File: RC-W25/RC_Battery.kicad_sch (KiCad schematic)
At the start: 18 parts, among them P1 JST CONN, SW1 Toggle Button, U2 MCP73831-5-OT, U3 AP62300TWU

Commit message: Began Routing
Only need to spec out buttons before completion
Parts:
- L1: footprint Inductor_SMD:ASPI-4030S-330M-T -> Inductor_SMD:L_Abracon_ASPI-4030S; LCSC# (none) -> C2050508
- renumbered R9 to R10, R10 to R11, R11 to R12, R12 to R13, R13 to R14, R8 to R9, SW1 to SW3
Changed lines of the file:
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@@
 		(on_board yes)
 		(dnp no)
-		(property "Reference" "#PWR028"
+		(property "Reference" "#PWR030"
 			(at 52.07 73.66 0)
 			(effects
@@
 			(project ""
 				(path "/427b2895-e3a6-4096-b101-5f65a3f7473e/9423f10d-7c89-4a48-b233-1b4f9ab13c89"
-					(reference "#PWR028")
+					(reference "#PWR030")
 					(unit 1)
 				)
@@
 		(on_board yes)
 		(dnp no)
-		(property "Reference" "R8"
+		(property "Reference" "R9"
 			(at 59.182 79.248 0)
 			(effects
@@
 			(project "RC-W25"
 				(path "/427b2895-e3a6-4096-b101-5f65a3f7473e/9423f10d-7c89-4a48-b233-1b4f9ab13c89"
-					(reference "R8")
+					(reference "R9")
 					(unit 1)
 				)
@@
 		(dnp no)
 		(fields_autoplaced yes)
-		(property "Reference" "#PWR027"
+		(property "Reference" "#PWR029"
 			(at 52.07 63.5 0)
 			(effects
@@
 			(project ""
 				(path "/427b2895-e3a6-4096-b101-5f65a3f7473e/9423f10d-7c89-4a48-b233-1b4f9ab13c89"
-					(reference "#PWR027")
+					(reference "#PWR029")
 					(unit 1)
 				)
@@
 		(dnp no)
 		(fields_autoplaced yes)
-		(property "Reference" "#PWR036"
+		(property "Reference" "#PWR038"
 			(at 176.53 133.35 0)
 			(effects
@@
 			(project "RC-W25"
 				(path "/427b2895-e3a6-4096-b101-5f65a3f7473e/9423f10d-7c89-4a48-b233-1b4f9ab13c89"
-					(reference "#PWR036")
+					(reference "#PWR038")
 					(unit 1)
 				)
@@
 		(dnp no)
 		(fields_autoplaced yes)
-		(property "Reference" "#PWR038"
+		(property "Reference" "#PWR040"
 			(at 223.52 137.16 0)
 			(effects
@@
 			(project "RC-W25"
 				(path "/427b2895-e3a6-4096-b101-5f65a3f7473e/9423f10d-7c89-4a48-b233-1b4f9ab13c89"
-					(reference "#PWR038")
+					(reference "#PWR040")
 					(unit 1)
 				)
@@
 		(on_board yes)
 		(dnp no)
-		(property "Reference" "#PWR035"
+		(property "Reference" "#PWR037"
 			(at 153.67 129.54 0)
 			(effects
@@
 			(project "RC-W25"
 				(path "/427b2895-e3a6-4096-b101-5f65a3f7473e/9423f10d-7c89-4a48-b233-1b4f9ab13c89"
-					(reference "#PWR035")
+					(reference "#PWR037")
 					(unit 1)
 				)
@@
 			)
 		)
-		(property "Footprint" "Inductor_SMD:ASPI-4030S-330M-T"
+		(property "Footprint" "Inductor_SMD:L_Abracon_ASPI-4030S"
 			(at 205.74 116.84 0)
 			(effects
@@
 			)
 		)
-		(property "Datasheet" "https://abracon.com/Magnetics/power/ASPI-4030S.pdf"
+		(property "Datasheet" "https://www.lcsc.com/datasheet/lcsc_datasheet_2410121520_Abracon-LLC-ASPI-4030S-3R3M-T_C2050508.pdf"
 			(at 205.74 116.84 0)
 			(effects
@@
 			)
 		)
-		(property "LCSC#" ""
+		(property "LCSC#" "C2050508"
 			(at 205.74 116.84 0)
 			(effects
@@
 		(dnp no)
 		(fields_autoplaced yes)
-		(property "Reference" "#PWR039"
+		(property "Reference" "#PWR041"
 			(at 234.95 116.84 0)
 			(effects
@@
 			(project "RC-W25"
 				(path "/427b2895-e3a6-4096-b101-5f65a3f7473e/9423f10d-7c89-4a48-b233-1b4f9ab13c89"
-					(reference "#PWR039")
+					(reference "#PWR041")
 					(unit 1)
 				)
@@
 		(on_board yes)
 		(dnp no)
-		(property "Reference" "R13"
+		(property "Reference" "R14"
 			(at 216.408 127.762 0)
 			(effects
@@
 			(project "RC-W25"
 				(path "/427b2895-e3a6-4096-b101-5f65a3f7473e/9423f10d-7c89-4a48-b233-1b4f9ab13c89"
-					(reference "R13")
+					(reference "R14")
 					(unit 1)
 				)
@@
 		(on_board yes)
 		(dnp no)
-		(property "Reference" "#PWR032"
+		(property "Reference" "#PWR034"
 			(at 128.27 97.79 0)
 			(effects
@@
 			(project "RC-W25"
 				(path "/427b2895-e3a6-4096-b101-5f65a3f7473e/9423f10d-7c89-4a48-b233-1b4f9ab13c89"
-					(reference "#PWR032")
+					(reference "#PWR034")
 					(unit 1)
 				)
@@
 		(on_board yes)
 		(dnp no)
-		(property "Reference" "R9"
+		(property "Reference" "R10"
 			(at 68.326 78.994 0)
 			(effects
@@
 			(project "RC-W25"
 				(path "/427b2895-e3a6-4096-b101-5f65a3f7473e/9423f10d-7c89-4a48-b233-1b4f9ab13c89"
-					(reference "R9")
+					(reference "R10")
 					(unit 1)
 				)
@@
 		(on_board yes)
 		(dnp no)
-		(property "Reference" "R10"
+		(property "Reference" "R11"
 			(at 123.698 75.692 0)
 			(effects
@@
 			(project "RC-W25"
 				(path "/427b2895-e3a6-4096-b101-5f65a3f7473e/9423f10d-7c89-4a48-b233-1b4f9ab13c89"
-					(reference "R10")
+					(reference "R11")
 					(unit 1)
 				)
@@
 		(dnp no)
 		(fields_autoplaced yes)
-		(property "Reference" "#PWR034"
+		(property "Reference" "#PWR036"
 			(at 147.32 118.11 0)
 			(effects
@@
 			(project "RC-W25"
 				(path "/427b2895-e3a6-4096-b101-5f65a3f7473e/9423f10d-7c89-4a48-b233-1b4f9ab13c89"
-					(reference "#PWR034")
+					(reference "#PWR036")
 					(unit 1)
 				)
@@
 		(on_board yes)
 		(dnp no)
-		(property "Reference" "SW1"
+		(property "Reference" "SW3"
 			(at 116.84 59.944 90)
 			(effects
@@
 			(project ""
 				(path "/427b2895-e3a6-4096-b101-5f65a3f7473e/9423f10d-7c89-4a48-b233-1b4f9ab13c89"
-					(reference "SW1")
+					(reference "SW3")
 					(unit 1)
 				)
@@
 		(on_board yes)
 		(dnp no)
-		(property "Reference" "R12"
+		(property "Reference" "R13"
 			(at 216.408 120.142 0)
 			(effects
@@
 			(project "RC-W25"
 				(path "/427b2895-e3a6-4096-b101-5f65a3f7473e/9423f10d-7c89-4a48-b233-1b4f9ab13c89"
-					(reference "R12")
+					(reference "R13")
 					(unit 1)
 				)
@@
 		(on_board yes)
 		(dnp no)
-		(property "Reference" "#PWR030"
+		(property "Reference" "#PWR032"
 			(at 105.41 83.82 0)
 			(effects
@@
 			(project "RC-W25"
 				(path "/427b2895-e3a6-4096-b101-5f65a3f7473e/9423f10d-7c89-4a48-b233-1b4f9ab13c89"
-					(reference "#PWR030")
+					(reference "#PWR032")
 					(unit 1)
 				)
@@
 		(on_board yes)
 		(dnp no)
-		(property "Reference" "#PWR029"
+		(property "Reference" "#PWR031"
 			(at 72.39 91.44 0)
 			(effects
@@
 			(project ""
 				(path "/427b2895-e3a6-4096-b101-5f65a3f7473e/9423f10d-7c89-4a48-b233-1b4f9ab13c89"
-					(reference "#PWR029")
+					(reference "#PWR031")
 					(unit 1)
 				)
@@
 		(on_board yes)
 		(dnp no)
-		(property "Reference" "#PWR031"
+		(property "Reference" "#PWR033"
 			(at 115.57 59.69 0)
 			(effects
@@
 			(project "RC-W25"
 				(path "/427b2895-e3a6-4096-b101-5f65a3f7473e/9423f10d-7c89-4a48-b233-1b4f9ab13c89"
-					(reference "#PWR031")
+					(reference "#PWR033")
 					(unit 1)
 				)
@@
 		(dnp no)
 		(fields_autoplaced yes)
-		(property "Reference" "#PWR037"
+		(property "Reference" "#PWR039"
 			(at 214.63 137.16 0)
 			(effects
@@
 			(project "RC-W25"
 				(path "/427b2895-e3a6-4096-b101-5f65a3f7473e/9423f10d-7c89-4a48-b233-1b4f9ab13c89"
-					(reference "#PWR037")
+					(reference "#PWR039")
 					(unit 1)
 				)
@@
 		(dnp no)
 		(fields_autoplaced yes)
-		(property "Reference" "#PWR040"
+		(property "Reference" "#PWR042"
 			(at 234.95 137.16 0)
 			(effects
@@
 			(project "RC-W25"
 				(path "/427b2895-e3a6-4096-b101-5f65a3f7473e/9423f10d-7c89-4a48-b233-1b4f9ab13c89"
-					(reference "#PWR040")
+					(reference "#PWR042")
 					(unit 1)
 				)
@@
 		(on_board yes)
 		(dnp no)
-		(property "Reference" "R11"
+		(property "Reference" "R12"
 			(at 123.698 85.598 0)
 			(effects
@@
 			(project "RC-W25"
 				(path "/427b2895-e3a6-4096-b101-5f65a3f7473e/9423f10d-7c89-4a48-b233-1b4f9ab13c89"
-					(reference "R11")
+					(reference "R12")
 					(unit 1)
 				)
@@
 		(on_board yes)
 		(dnp no)
-		(property "Reference" "#PWR053"
+		(property "Reference" "#PWR035"
 			(at 140.97 78.74 0)
 			(effects
@@
 			(project "RC-W25"
 				(path "/427b2895-e3a6-4096-b101-5f65a3f7473e/9423f10d-7c89-4a48-b233-1b4f9ab13c89"
-					(reference "#PWR053")
-					(unit 1)
-				)
+					(reference "#PWR035")
+					(unit 1)
+				)

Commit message: EM Custom RC V1
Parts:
- removed SW3: Toggle Button, symbol Switch:SW_SPST
- added SW5: YTSPS-22E58LM, footprints:SW-SMD_6P-YTSPS-22E58LM, symbol components:YTSPS-22E58LM
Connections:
- net +VBAT: now also SW5.2
- net at C11.1, P1.1 (Pin_1), R11.1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: now also SW5.3
- no-connect marks 1 -> 5

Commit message: crc v1
finalized!! finally!! yes!!

- spec out 3.7V 1000mAh cell
- spec out ultra-thin coin motor

^make sure they have a jst-ph male connector or are organized to be ordered alongside one for manual soldering.
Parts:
- P1: footprint Library:CONN02_502352_MOL -> footprints:CONN-SMD_2P-P2.00_XUNPU_WAFER-PH2.0-2PWB; LCSC# (none) -> C3029440
- renumbered SW5 to SW3
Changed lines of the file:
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@@
 			)
 		)
-		(property "Footprint" "Library:CONN02_502352_MOL"
+		(property "Footprint" "footprints:CONN-SMD_2P-P2.00_XUNPU_WAFER-PH2.0-2PWB"
 			(at 146.05 69.85 0)
 			(effects
@@
 			)
 		)
-		(property "Datasheet" "~"
+		(property "Datasheet" "https://www.lcsc.com/datasheet/lcsc_datasheet_2411192313_XUNPU-WAFER-PH2-0-2PWB_C3029440.pdf"
 			(at 146.05 69.85 0)
 			(effects
@@
 			)
 		)
-		(property "LCSC#" ""
+		(property "LCSC#" "C3029440"
 			(at 146.05 69.85 0)
 			(effects
@@
 		(on_board yes)
 		(dnp no)
-		(property "Reference" "SW5"
+		(property "Reference" "SW3"
 			(at 126.746 60.452 90)
 			(effects
@@
 			(project ""
 				(path "/427b2895-e3a6-4096-b101-5f65a3f7473e/9423f10d-7c89-4a48-b233-1b4f9ab13c89"
-					(reference "SW5")
-					(unit 1)
-				)
+					(reference "SW3")
+					(unit 1)
+				)

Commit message: crc v1
quick fixes
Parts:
- L1: footprint Inductor_SMD:L_Abracon_ASPI-4030S -> footprints:L_Abracon_ASPI-4030S
- R11: value 42k -> 36.6k
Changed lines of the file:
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@@
 	)
 	(symbol
-		(lib_id "power:GND")
+		(lib_id "power:Earth")
 		(at 52.07 67.31 0)
 		(unit 1)
@@
 			)
 		)
-		(property "Datasheet" ""
+		(property "Datasheet" "~"
 			(at 52.07 67.31 0)
 			(effects
@@
 			)
 		)
-		(property "Description" "Power symbol creates a global label with name \"GND\" , ground"
+		(property "Description" "Power symbol creates a global label with name \"Earth\""
 			(at 52.07 67.31 0)
 			(effects
@@
 	)
 	(symbol
-		(lib_id "power:GND")
+		(lib_id "power:Earth")
 		(at 176.53 127 0)
 		(unit 1)
@@
 		)
 		(property "Value" "GND"
-			(at 176.53 132.08 0)
-			(effects
-				(font
-					(size 1.27 1.27)
-				)
+			(at 179.07 128.2699 0)
+			(effects
+				(font
+					(size 1.27 1.27)
+				)
+				(justify left)
 			)
 		)
@@
 			)
 		)
-		(property "Datasheet" ""
+		(property "Datasheet" "~"
 			(at 176.53 127 0)
 			(effects
@@
 			)
 		)
-		(property "Description" "Power symbol creates a global label with name \"GND\" , ground"
+		(property "Description" "Power symbol creates a global label with name \"Earth\""
 			(at 176.53 127 0)
 			(effects
@@
 	)
 	(symbol
-		(lib_id "power:GND")
+		(lib_id "power:Earth")
 		(at 223.52 130.81 0)
 		(unit 1)
@@
 		)
 		(property "Value" "GND"
-			(at 223.52 135.89 0)
-			(effects
-				(font
-					(size 1.27 1.27)
-				)
+			(at 226.06 132.0799 0)
+			(effects
+				(font
+					(size 1.27 1.27)
+				)
+				(justify left)
 			)
 		)
@@
 			)
 		)
-		(property "Datasheet" ""
+		(property "Datasheet" "~"
 			(at 223.52 130.81 0)
 			(effects
@@
 			)
 		)
-		(property "Description" "Power symbol creates a global label with name \"GND\" , ground"
+		(property "Description" "Power symbol creates a global label with name \"Earth\""
 			(at 223.52 130.81 0)
 			(effects
@@
 	)
 	(symbol
-		(lib_id "power:GND")
+		(lib_id "power:Earth")
 		(at 153.67 123.19 0)
 		(unit 1)
@@
 			)
 		)
-		(property "Datasheet" ""
+		(property "Datasheet" "~"
 			(at 153.67 123.19 0)
 			(effects
@@
 			)
 		)
-		(property "Description" "Power symbol creates a global label with name \"GND\" , ground"
+		(property "Description" "Power symbol creates a global label with name \"Earth\""
 			(at 153.67 123.19 0)
 			(effects
@@
 			)
 		)
-		(property "Footprint" "Inductor_SMD:L_Abracon_ASPI-4030S"
+		(property "Footprint" "footprints:L_Abracon_ASPI-4030S"
 			(at 205.74 116.84 0)
 			(effects
@@
 	)
 	(symbol
-		(lib_id "power:GND")
+		(lib_id "power:Earth")
 		(at 128.27 91.44 0)
 		(unit 1)
@@
 			)
 		)
-		(property "Datasheet" ""
+		(property "Datasheet" "~"
 			(at 128.27 91.44 0)
 			(effects
@@
 			)
 		)
-		(property "Description" "Power symbol creates a global label with name \"GND\" , ground"
+		(property "Description" "Power symbol creates a global label with name \"Earth\""
 			(at 128.27 91.44 0)
 			(effects
@@
 			)
 		)
-		(property "Value" "42k"
+		(property "Value" "36.6k"
 			(at 123.698 77.47 0)
 			(effects
@@
 	)
 	(symbol
-		(lib_id "power:GND")
+		(lib_id "power:Earth")
 		(at 105.41 77.47 0)
 		(unit 1)
@@
 			)
 		)
-		(property "Datasheet" ""
+		(property "Datasheet" "~"
 			(at 105.41 77.47 0)
 			(effects
@@
 			)
 		)
-		(property "Description" "Power symbol creates a global label with name \"GND\" , ground"
+		(property "Description" "Power symbol creates a global label with name \"Earth\""
 			(at 105.41 77.47 0)
 			(effects
@@
 	)
 	(symbol
-		(lib_id "power:GND")
+		(lib_id "power:Earth")
 		(at 72.39 85.09 0)
 		(unit 1)
@@
 			)
 		)
-		(property "Datasheet" ""
+		(property "Datasheet" "~"
 			(at 72.39 85.09 0)
 			(effects
@@
 			)
 		)
-		(property "Description" "Power symbol creates a global label with name \"GND\" , ground"
+		(property "Description" "Power symbol creates a global label with name \"Earth\""
 			(at 72.39 85.09 0)
 			(effects
@@
 	)
 	(symbol
-		(lib_id "power:GND")
+		(lib_id "power:Earth")
 		(at 214.63 130.81 0)
 		(unit 1)
@@
 		)
 		(property "Value" "GND"
-			(at 214.63 135.89 0)
-			(effects
-				(font
-					(size 1.27 1.27)
-				)
+			(at 217.17 132.0799 0)
+			(effects
+				(font
+					(size 1.27 1.27)
+				)
+				(justify left)
 			)
 		)
@@
 			)
 		)
-		(property "Datasheet" ""
+		(property "Datasheet" "~"
 			(at 214.63 130.81 0)
 			(effects
@@
 			)
 		)
-		(property "Description" "Power symbol creates a global label with name \"GND\" , ground"
+		(property "Description" "Power symbol creates a global label with name \"Earth\""
 			(at 214.63 130.81 0)
 			(effects
@@
 	)
 	(symbol
-		(lib_id "power:GND")
+		(lib_id "power:Earth")
 		(at 234.95 130.81 0)
 		(unit 1)
@@
 		)
 		(property "Value" "GND"
-			(at 234.95 135.89 0)
-			(effects
-				(font
-					(size 1.27 1.27)
-				)
+			(at 237.49 132.0799 0)
+			(effects
+				(font
+					(size 1.27 1.27)
+				)
+				(justify left)
 			)
 		)
@@
 			)
 		)
-		(property "Datasheet" ""
+		(property "Datasheet" "~"
 			(at 234.95 130.81 0)
 			(effects
@@
 			)
 		)
-		(property "Description" "Power symbol creates a global label with name \"GND\" , ground"
+		(property "Description" "Power symbol creates a global label with name \"Earth\""
 			(at 234.95 130.81 0)
 			(effects
@@
 	)
 	(symbol
-		(lib_id "power:GND")
+		(lib_id "power:Earth")
 		(at 140.97 72.39 0)
 		(unit 1)
@@
 			)
 		)
-		(property "Datasheet" ""
+		(property "Datasheet" "~"
 			(at 140.97 72.39 0)
 			(effects
@@
 			)
 		)
-		(property "Description" "Power symbol creates a global label with name \"GND\" , ground"
+		(property "Description" "Power symbol creates a global label with name \"Earth\""
 			(at 140.97 72.39 0)
 			(effects

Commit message: crc v2
finalizing receiver layout
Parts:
- R13: value 33.2k -> 2.7k
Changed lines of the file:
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@@
 			)
 		)
-		(property "Value" "33.2k"
+		(property "Value" "2.7k"
 			(at 216.408 121.9201 0)
 			(effects

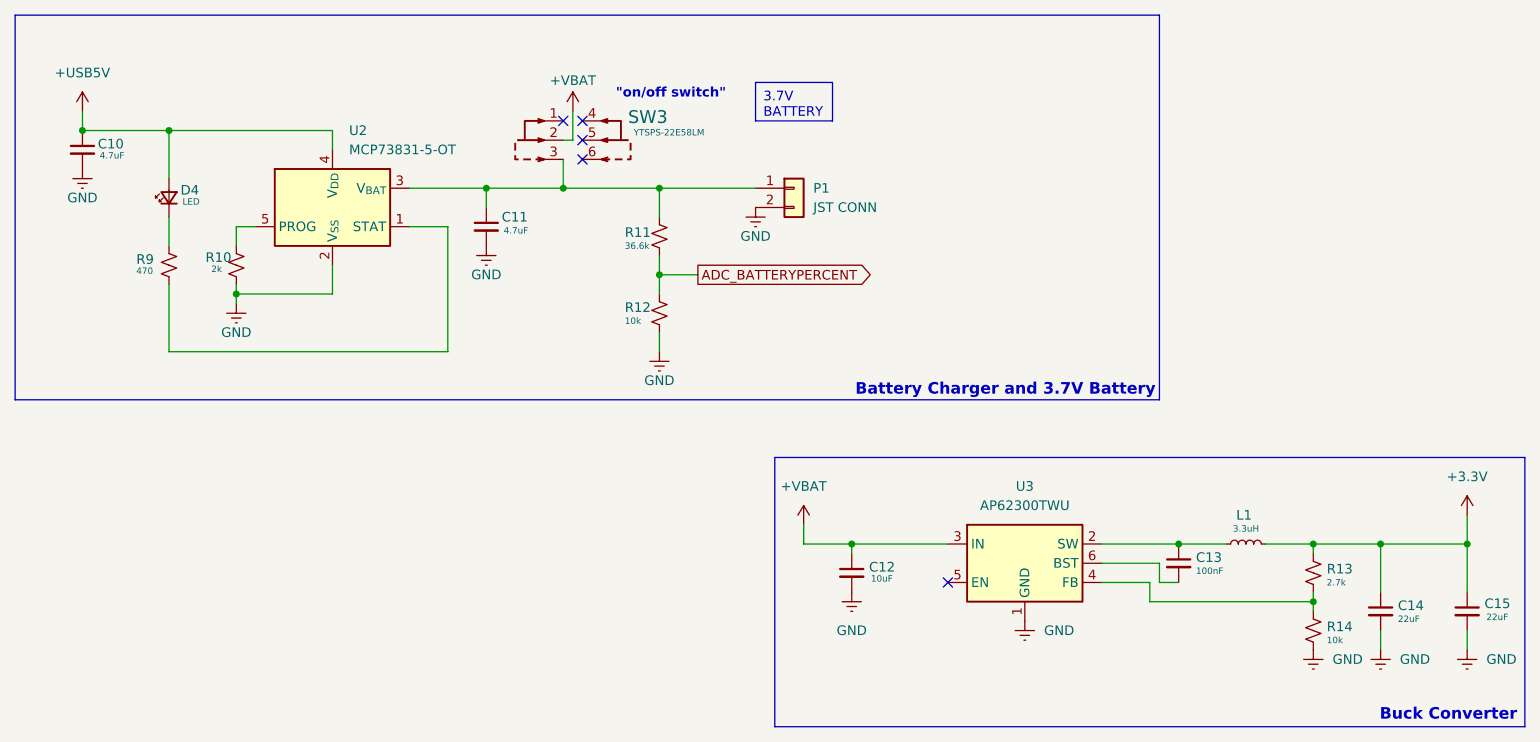
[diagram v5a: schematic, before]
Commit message: crc v2
remote and receiver complete! assembly and orders have been prepared for purchasing.
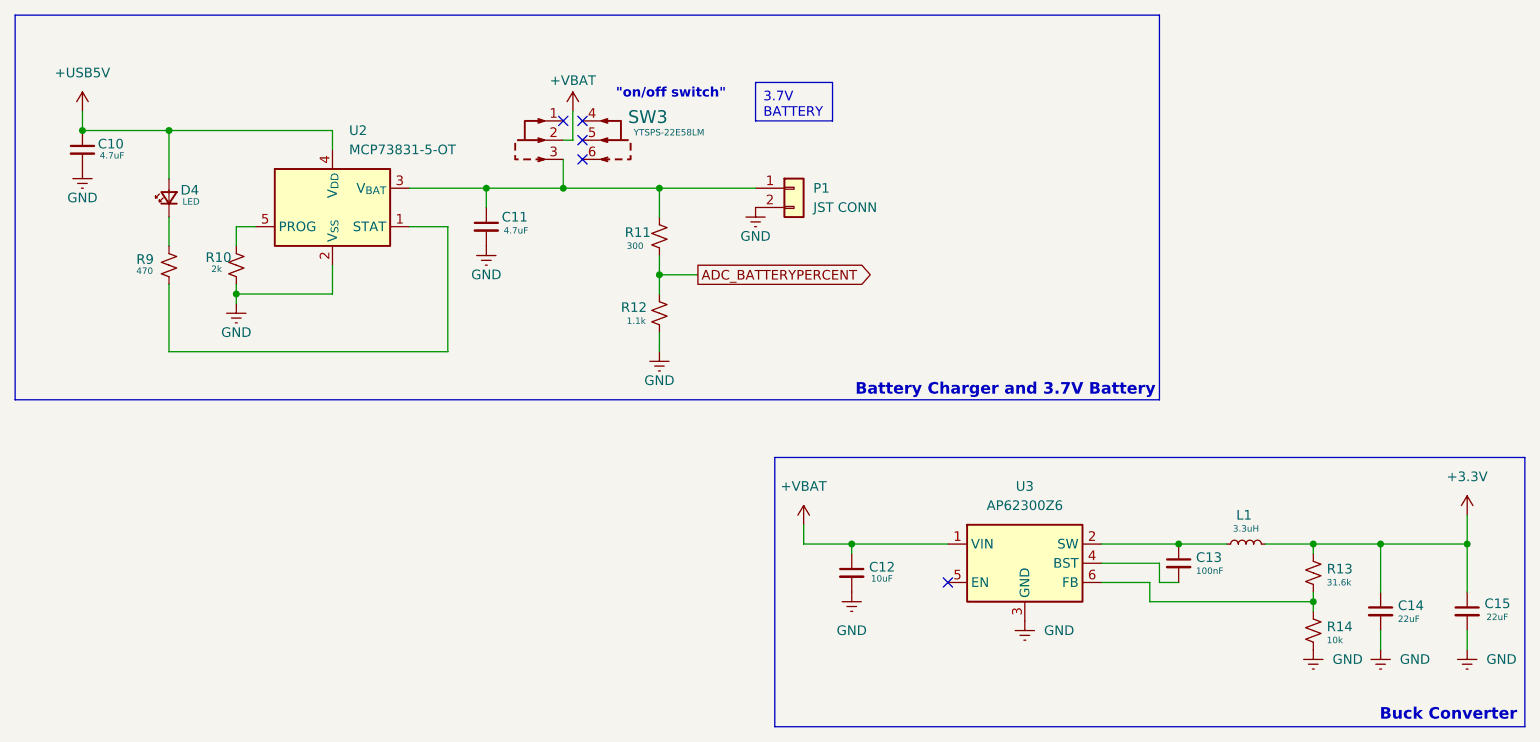
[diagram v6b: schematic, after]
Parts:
- removed U3: AP62300TWU, Package_TO_SOT_SMD:TSOT-23-6, symbol Regulator_Switching:AP62300TWU
- added U3: AP62300Z6, Package_TO_SOT_SMD:SOT-563, symbol Regulator_Switching:AP62300Z6
- C10, C11: LCSC# C22399610 -> C23733; MPN (none) -> C23733
- C12: MPN (none) -> C95839
- C13: LCSC# C22435938 -> C1525; MPN (none) -> C1525
- C14, C15: LCSC# C380337 -> C87997; MPN (none) -> C87997
- D4: footprint Diode_SMD:D_0402_1005Metric -> footprints:D_0402_1005Metric; LCSC# C7496801 -> C131223; MPN (none) -> C131223
- L1: LCSC# C2050508 -> C15269; MPN (none) -> C2050508
- P1: MPN (none) -> C3029440
- R10: MPN (none) -> C2902640
- R11: value 36.6k -> 300; LCSC# C5137149 -> C852712; MPN (none) -> C852712
- R12: value 10k -> 1.1k; LCSC# C190095 -> C445597; MPN (none) -> C445597
- R13: value 2.7k -> 31.6k; LCSC# C2681602 -> C782222; MPN (none) -> C782222
- R14: MPN (none) -> C190095
- R9: MPN (none) -> C852799
- SW3: MPN (none) -> C2941005
- U2: MPN (none) -> C635037
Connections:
- net +VBAT: now also U3.1 (VIN)
- net GND: now also U3.3 (GND)
- net at C13.1, L1.1: now also U3.2 (SW)
- net at R13.2, R14.1: now also U3.6 (FB)
- net at C13.2: now also U3.4 (BST)
